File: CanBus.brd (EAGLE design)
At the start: 80 x 100 mm, 23 parts, among them IC1 MCP2515-I/SO, IC2 MEGA8-P, IC3 MCP2515-I/SO, Q1 16MHz, Q2 16MHz, U1 MCP2562-E/P, U2 MCP2562-E/P, X1 MAC64L

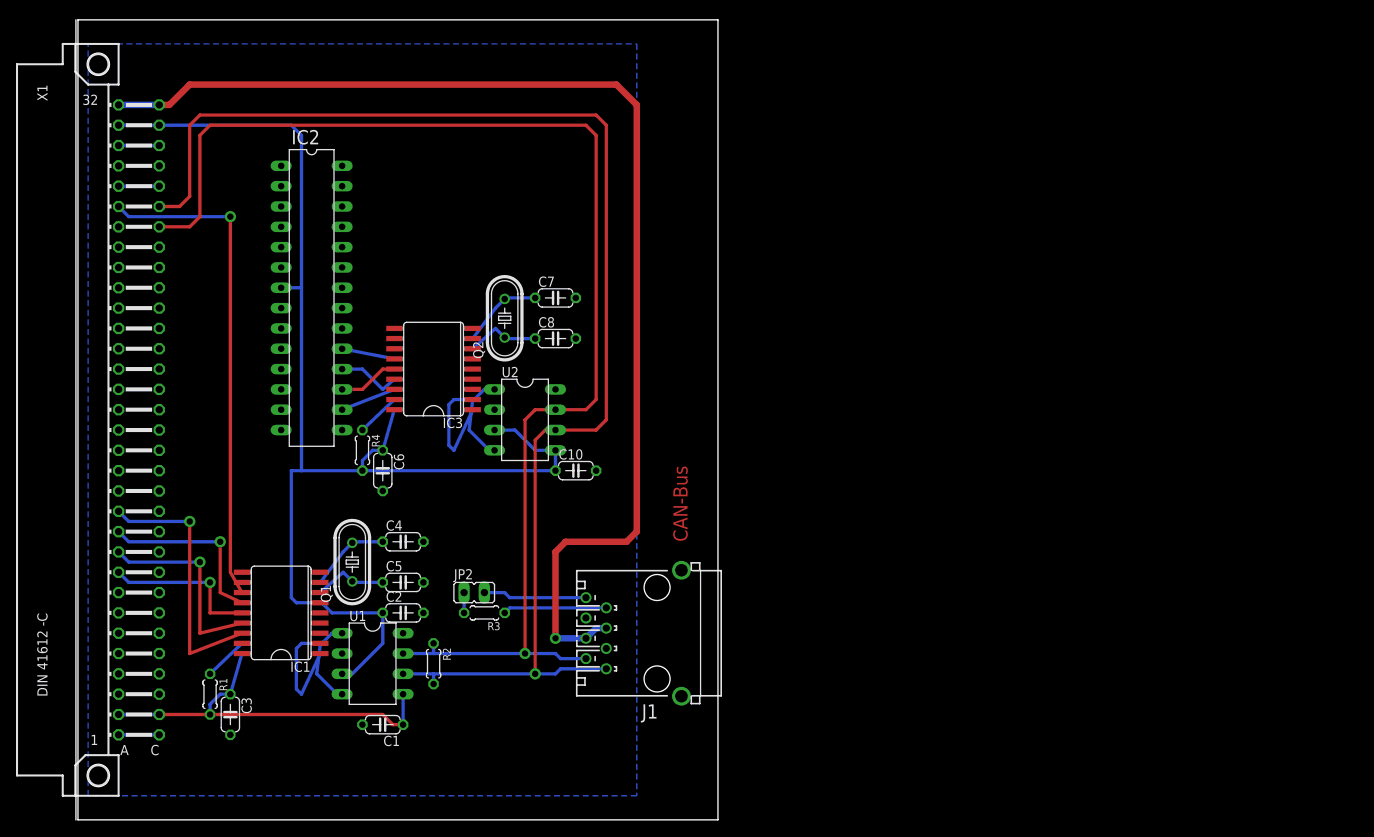
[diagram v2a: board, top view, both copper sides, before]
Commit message: Pi, CanBus, Stromversorgung, Steckverbinder angepasst
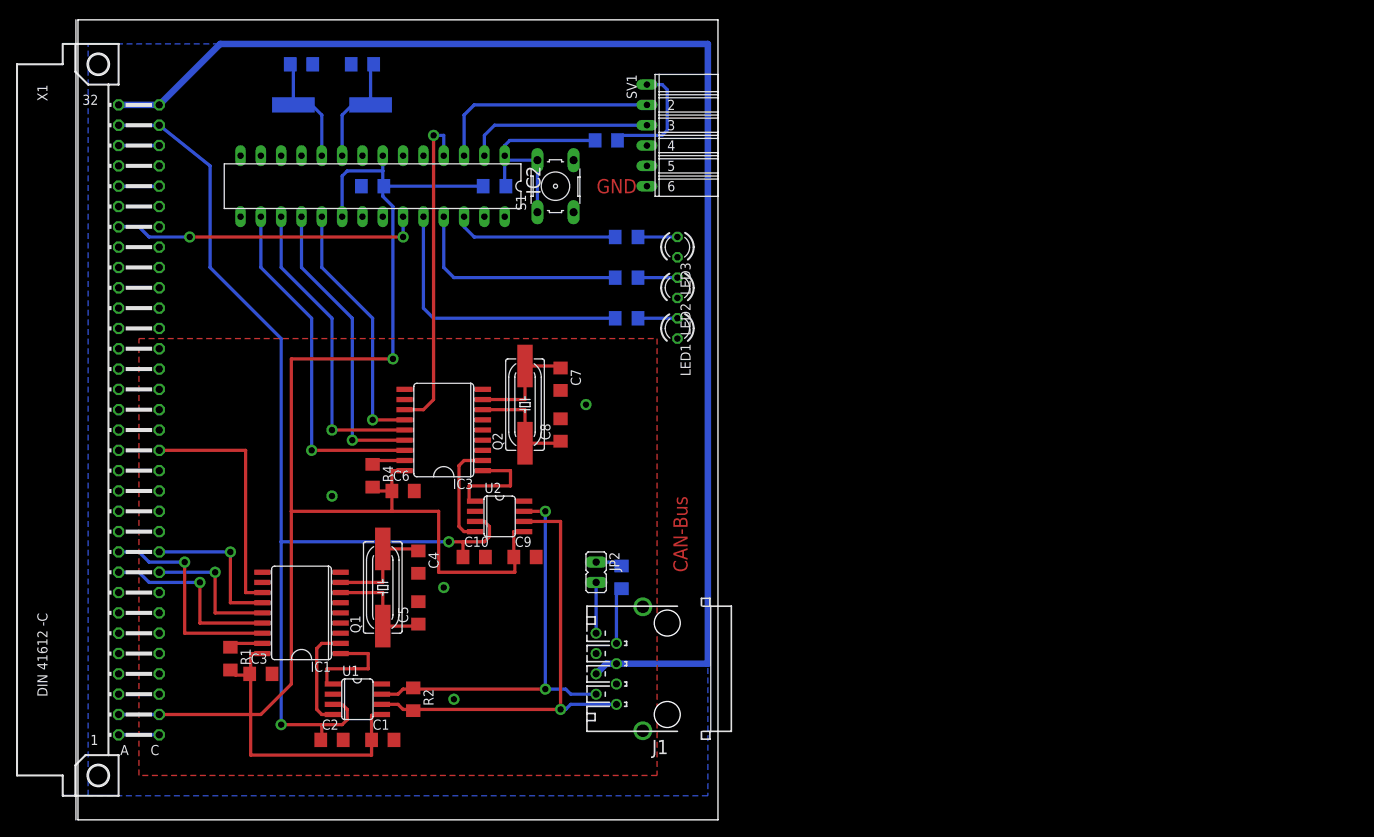
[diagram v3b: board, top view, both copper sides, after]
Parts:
- added C11, C12, C9: 100nF, rcl:C1206
- added C13, C14: 22pF, rcl:C1206
- added LED1, LED2, LED3: 2mA, led:LED3MM
- added Q3: 16MHz, crystal:HC49UP
- added R5: 10k, rcl:R1206
- added R6, R7, R8: 560R, rcl:R1206
- added S1: (no value), switch-omron:B3F-10XX
- added SV1: (no value), con-lsta:FE06W
- C1, C10, C2, C3, C4, C5, C6, C7, C8: device rcl:C050-024X044 -> rcl:C1206
- J1: device con-amp:555153-1 -> mebp_8-8g:MEBP_8-8G
- Q1, Q2: device crystal:HC49/S -> crystal:HC49UP
- R1, R2, R3, R4: device rcl:0204/5 -> rcl:R1206
- U1, U2: value MCP2562-E/P -> MCP2562-E/SN; device mcp2515_2551_2562:DIL8 -> mcp2515_2551_2562:SO08
- moved C2 18.2 mm to (31.8, 9.53)
- moved R3 17.7 mm to (67.9, 29.8), flipped to the bottom, turned to 90 degrees
- moved C10 16.7 mm to (49.5, 32.4)
- moved IC2 15.9 mm to (36.8, 78.7), turned to 180 degrees
- moved JP2 15.5 mm to (64.8, 30.5), turned to 180 degrees
- moved U2 13.5 mm to (52.7, 37.5)
- moved C8 11.4 mm to (60.3, 48.3), turned to 90 degrees
- moved Q2 11.1 mm to (55.9, 51.4)
- moved C7 10.2 mm to (60.3, 54.6), turned to 270 degrees
- moved IC3 7.73 mm to (45.7, 48.3)
- moved U1 6.54 mm to (34.9, 14.6)
- moved C3 6.35 mm to (22.9, 17.8), turned to 0 degrees
- moved R2 5.12 mm to (41.9, 14.6)
- moved R1 5.12 mm to (19.1, 19.7)
- moved Q1 4.96 mm to (38.1, 28.6)
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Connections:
- removed net AVCC: IC2.20
- new net AT_INT0: IC2.4, IC3.12
- new net LED1: IC2.24, R6.2
- new net LED2: IC2.25, R7.2
- new net LED3: IC2.26, R8.2
- new net N$10: C13.2, IC2.9, Q3.2
- new net N$11: C14.2, IC2.10, Q3.1
- new net N$12: C13.1, C14.1
- new net N$14: LED1.A, R6.1
- new net N$15: LED2.A, R7.1
- new net N$19: LED3.A, R8.1
- new net N$8: C11.2, IC2.1, R5.1, S1.1, S1.2
- new net PROG_DTR: C11.1, SV1.1
- new net PROG_RX: IC2.3, SV1.2
- new net PROG_TX: IC2.2, SV1.3
- net !PI_RESET: now also IC2.23, X1.A26; no longer X1.C7
- net +3,3V: now also C12.2, C6.1, C9.1, IC2.20, IC2.7, IC3.18, R4.2, R5.2, U2.5
- net +5V_EXT: no longer C6.1, IC2.7, IC3.18, R4.2, U2.5
- net CANH: no longer X1.C26
- net CANL: no longer X1.C27
- net GND: now also C12.1, C9.2, J1.G1, J1.G2, LED1.K, LED2.K, LED3.K, S1.3, S1.4, SV1.6
- net GPIO.05: now also X1.C14; no longer X1.A14
- net GPIO.06: now also IC1.12, X1.C15; no longer X1.A15
- net GPIO.12: now also X1.C16; no longer X1.A16
- net GPIO.13: now also X1.C17; no longer X1.A17
- net GPIO.16: now also X1.C18; no longer X1.A18
- net GPIO.17: now also X1.C19; no longer X1.A19
- net GPIO.18: now also X1.C20; no longer X1.A20
- net GPIO.19: now also X1.C21; no longer X1.A21
- net GPIO.20: now also X1.C22; no longer X1.A22
- net GPIO.21: now also X1.C23; no longer X1.A23
- net GPIO.22: now also X1.C24; no longer X1.A24
- net GPIO.23: now also X1.C25; no longer X1.A25
- net GPIO.24: now also X1.C26; no longer X1.A26
- net GPIO.25: now also X1.C27; no longer IC1.12, X1.A27
- net RXD: now also X1.C12; no longer X1.C25
- net SPI_CE0: now also X1.A10; no longer X1.A12
- net SPI_CE1: now also X1.C11; no longer X1.A13
- net SPI_MISO: now also X1.A9; no longer X1.A10
- net SPI_MOSI: now also X1.C9; no longer X1.A9
- net SPI_SCLK: now also X1.C10; no longer X1.A11
- net TXD: now also X1.A12; no longer X1.C24
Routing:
- net +3,3V: track 49.5 -> 215.2 mm, vias 0 -> 1
- net CANL: track 169.3 -> 58.0 mm
- net CANH: track 162.9 -> 52.4 mm, vias 1 -> 2
- net GPIO.25: track 61.9 -> 0.00 mm, vias 1 -> 0
- net AT_INT0: track 0.00 -> 41.0 mm, vias 0 -> 1
- net !PI_RESET: track 0.00 -> 38.6 mm, vias 0 -> 2
- net AT_SPI_CS: track 7.00 -> 43.4 mm, vias 0 -> 1
- net LED1: track 0.00 -> 35.9 mm
- net AT_SPI_MOSI: track 7.58 -> 38.4 mm, vias 0 -> 1
- net GPIO.06: track 0.00 -> 30.7 mm
- net +5V_EXT: track 160.2 -> 130.9 mm, vias 0 -> 2
- net AT_SPI_MISO: track 8.06 -> 37.1 mm, vias 0 -> 1
- net PROG_RX: track 0.00 -> 28.5 mm
- net LED2: track 0.00 -> 28.3 mm
- net N$8: track 0.00 -> 27.8 mm
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- added copper zone on layer 1, net GND
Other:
- board text added: "GND"

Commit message: Platinen angepasst, Backplane
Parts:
- added JP1, JP10, JP3, JP4, JP5, JP6, JP7, JP8, JP9: (no value), pinhead:1X01
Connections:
- new net AT_PB0: IC2.14, JP9.1
- new net AT_PB1: IC2.15, JP10.1
- new net AT_PC4: IC2.27, JP1.1
- new net AT_PC5: IC2.28, JP3.1
- new net AT_PD3: IC2.5, JP4.1
- new net AT_PD4: IC2.6, JP5.1
- new net AT_PD5: IC2.11, JP6.1
- new net AT_PD6: IC2.12, JP7.1
- new net AT_PD7: IC2.13, JP8.1
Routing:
- net AT_PD5: track 0.00 -> 14.3 mm
- net AT_PD6: track 0.00 -> 10.7 mm
- net !PI_RESET: track 38.6 -> 44.8 mm
- net LED3: track 20.7 -> 25.2 mm
- net AT_PD7: track 0.00 -> 3.81 mm
- net AT_PD4: track 0.00 -> 3.81 mm
- net AT_PD3: track 0.00 -> 3.81 mm
- net AT_PC5: track 0.00 -> 3.81 mm
- net AT_PC4: track 0.00 -> 3.81 mm
- net AT_PB1: track 0.00 -> 3.81 mm
- net AT_PB0: track 0.00 -> 3.81 mm
- net AT_INT0: track 41.0 -> 42.0 mm
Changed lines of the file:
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@@
 <attribute name="MF" value="" x="59.69" y="78.74" size="1.778" layer="27" rot="R90" display="off"/>
 </element>
+<element name="JP1" library="pinhead" package="1X01" value="" x="50.8" y="71.12"/>
+<element name="JP3" library="pinhead" package="1X01" value="" x="53.34" y="71.12"/>
+<element name="JP4" library="pinhead" package="1X01" value="" x="43.18" y="86.36"/>
+<element name="JP5" library="pinhead" package="1X01" value="" x="40.64" y="86.36"/>
+<element name="JP6" library="pinhead" package="1X01" value="" x="16.51" y="77.47"/>
+<element name="JP7" library="pinhead" package="1X01" value="" x="16.51" y="80.01"/>
+<element name="JP8" library="pinhead" package="1X01" value="" x="22.86" y="86.36"/>
+<element name="JP9" library="pinhead" package="1X01" value="" x="20.32" y="86.36"/>
+<element name="JP10" library="pinhead" package="1X01" value="" x="20.32" y="71.12"/>
 </elements>
 <signals>
@@
 <contactref element="C10" pad="1"/>
 <contactref element="U2" pad="3"/>
-<wire x1="25.4" y1="34.29" x2="25.4" y2="59.69" width="0.4064" layer="16"/>
-<wire x1="25.4" y1="59.69" x2="16.51" y2="68.58" width="0.4064" layer="16"/>
-<wire x1="16.51" y1="68.58" x2="16.51" y2="81.28" width="0.4064" layer="16"/>
+<wire x1="25.4" y1="34.29" x2="25.4" y2="60.96" width="0.4064" layer="16"/>
+<wire x1="25.4" y1="60.96" x2="12.7" y2="73.66" width="0.4064" layer="16"/>
 <wire x1="49.6316" y1="36.83" x2="50.8" y2="36.83" width="0.4064" layer="1"/>
 <wire x1="50.8" y1="36.83" x2="51.435" y2="36.195" width="0.4064" layer="1"/>
@@
 <via x="46.355" y="34.29" extent="1-16" drill="0.8" diameter="1.4224"/>
 <wire x1="46.355" y1="34.29" x2="25.4" y2="34.29" width="0.4064" layer="16"/>
-<wire x1="16.51" y1="81.28" x2="10.16" y2="86.36" width="0.4064" layer="16"/>
+<wire x1="12.7" y1="73.66" x2="12.7" y2="83.82" width="0.4064" layer="16"/>
+<wire x1="12.7" y1="83.82" x2="10.16" y2="86.36" width="0.4064" layer="16"/>
 <wire x1="33.02" y1="13.97" x2="31.8516" y2="13.97" width="0" layer="19" extent="1-1"/>
 </signal>
@@
 <wire x1="5.08" y1="73.66" x2="7.62" y2="73.66" width="0.4064" layer="16"/>
 <wire x1="7.62" y1="73.66" x2="8.89" y2="72.39" width="0.4064" layer="16"/>
-<wire x1="8.89" y1="72.39" x2="13.97" y2="72.39" width="0.4064" layer="16"/>
-<via x="13.97" y="72.39" extent="1-16" drill="0.8" diameter="1.4224"/>
-<wire x1="13.97" y1="72.39" x2="40.64" y2="72.39" width="0.4064" layer="1"/>
-<via x="40.64" y="72.39" extent="1-16" drill="0.8" diameter="1.4224"/>
-<wire x1="40.64" y1="72.39" x2="40.64" y2="74.93" width="0.4064" layer="16"/>
+<wire x1="8.89" y1="72.39" x2="11.43" y2="72.39" width="0.4064" layer="16"/>
+<wire x1="11.43" y1="72.39" x2="13.97" y2="69.85" width="0.4064" layer="16"/>
+<wire x1="13.97" y1="69.85" x2="13.97" y2="68.58" width="0.4064" layer="16"/>
+<via x="13.97" y="68.58" extent="1-16" drill="0.8" diameter="1.4224"/>
+<wire x1="13.97" y1="68.58" x2="40.64" y2="68.58" width="0.4064" layer="1"/>
+<via x="40.64" y="68.58" extent="1-16" drill="0.8" diameter="1.4224"/>
+<wire x1="40.64" y1="68.58" x2="40.64" y2="74.93" width="0.4064" layer="16"/>
 </signal>
 <signal name="GND">
@@
 <contactref element="S1" pad="3"/>
 <contactref element="S1" pad="4"/>
+<via x="49.53" y="55.88" extent="1-16" drill="0.8" diameter="1.4224"/>
+<via x="31.75" y="33.02" extent="1-16" drill="0.8" diameter="1.4224"/>
 <wire x1="49.6316" y1="38.1" x2="50.93" y2="32.385" width="0" layer="19" extent="1-1"/>
 </signal>
@@
 <contactref element="IC2" pad="4"/>
 <wire x1="40.8178" y1="50.8" x2="43.18" y2="50.8" width="0.4064" layer="1"/>
-<wire x1="43.18" y1="50.8" x2="44.45" y2="52.07" width="0.4064" layer="1"/>
-<wire x1="44.45" y1="52.07" x2="44.45" y2="85.09" width="0.4064" layer="1"/>
-<via x="44.45" y="85.09" extent="1-16" drill="0.8" diameter="1.4224"/>
-<wire x1="44.45" y1="85.09" x2="45.72" y2="85.09" width="0.4064" layer="16"/>
+<wire x1="43.18" y1="50.8" x2="46.99" y2="54.61" width="0.4064" layer="1"/>
+<wire x1="46.99" y1="54.61" x2="46.99" y2="85.09" width="0.4064" layer="1"/>
+<via x="46.99" y="85.09" extent="1-16" drill="0.8" diameter="1.4224"/>
+<wire x1="46.99" y1="85.09" x2="45.72" y2="85.09" width="0.4064" layer="16"/>
 <wire x1="45.72" y1="85.09" x2="45.72" y2="82.55" width="0.4064" layer="16"/>
 </signal>
@@
 <contactref element="R8" pad="2"/>
 <contactref element="IC2" pad="26"/>
-<wire x1="67.158" y1="72.39" x2="49.53" y2="72.39" width="0.4064" layer="16"/>
-<wire x1="49.53" y1="72.39" x2="48.26" y2="73.66" width="0.4064" layer="16"/>
-<wire x1="48.26" y1="73.66" x2="48.26" y2="74.93" width="0.4064" layer="16"/>
+<wire x1="67.158" y1="72.39" x2="66.04" y2="72.39" width="0.4064" layer="16"/>
+<wire x1="66.04" y1="72.39" x2="62.865" y2="69.215" width="0.4064" layer="16"/>
+<wire x1="62.865" y1="69.215" x2="49.53" y2="69.215" width="0.4064" layer="16"/>
+<wire x1="49.53" y1="69.215" x2="48.26" y2="70.485" width="0.4064" layer="16"/>
+<wire x1="48.26" y1="70.485" x2="48.26" y2="74.93" width="0.4064" layer="16"/>
 </signal>
 <signal name="N$14">
@@
 <wire x1="45.72" y1="68.58" x2="45.72" y2="74.93" width="0.4064" layer="16"/>
 </signal>
+<signal name="AT_PD5">
+<contactref element="IC2" pad="11"/>
+<contactref element="JP6" pad="1"/>
+<wire x1="27.94" y1="82.55" x2="27.94" y2="81.28" width="0.4064" layer="16"/>
+<wire x1="27.94" y1="81.28" x2="24.13" y2="77.47" width="0.4064" layer="16"/>
+<wire x1="24.13" y1="77.47" x2="16.51" y2="77.47" width="0.4064" layer="16"/>
+</signal>
+<signal name="AT_PD6">
+<contactref element="IC2" pad="12"/>
+<contactref element="JP7" pad="1"/>
+<wire x1="25.4" y1="82.55" x2="25.4" y2="81.28" width="0.4064" layer="16"/>
+<wire x1="25.4" y1="81.28" x2="24.13" y2="80.01" width="0.4064" layer="16"/>
+<wire x1="24.13" y1="80.01" x2="16.51" y2="80.01" width="0.4064" layer="16"/>
+</signal>
+<signal name="AT_PD7">
+<contactref element="IC2" pad="13"/>
+<contactref element="JP8" pad="1"/>
+<wire x1="22.86" y1="82.55" x2="22.86" y2="86.36" width="0.4064" layer="16"/>
+</signal>
+<signal name="AT_PB0">
+<contactref element="IC2" pad="14"/>
+<contactref element="JP9" pad="1"/>
+<wire x1="20.32" y1="82.55" x2="20.32" y2="86.36" width="0.4064" layer="16"/>
+</signal>
+<signal name="AT_PB1">
+<contactref element="IC2" pad="15"/>
+<contactref element="JP10" pad="1"/>
+<wire x1="20.32" y1="74.93" x2="20.32" y2="71.12" width="0.4064" layer="16"/>
+</signal>
+<signal name="AT_PD3">
+<contactref element="IC2" pad="5"/>
+<contactref element="JP4" pad="1"/>
+<wire x1="43.18" y1="82.55" x2="43.18" y2="86.36" width="0.4064" layer="16"/>
+</signal>
+<signal name="AT_PD4">
+<contactref element="IC2" pad="6"/>
+<contactref element="JP5" pad="1"/>
+<wire x1="40.64" y1="82.55" x2="40.64" y2="86.36" width="0.4064" layer="16"/>
+</signal>
+<signal name="AT_PC4">
+<contactref element="IC2" pad="27"/>
+<contactref element="JP1" pad="1"/>
+<wire x1="50.8" y1="74.93" x2="50.8" y2="71.12" width="0.4064" layer="16"/>
+</signal>
+<signal name="AT_PC5">
+<contactref element="IC2" pad="28"/>
+<contactref element="JP3" pad="1"/>
+<wire x1="53.34" y1="74.93" x2="53.34" y2="71.12" width="0.4064" layer="16"/>
+</signal>
 </signals>
